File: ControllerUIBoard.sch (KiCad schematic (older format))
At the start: 32 parts

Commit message: - Earth durch GND an den letzten Stellen ersetzt
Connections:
- net labels removed: Earth
- wire segments 131 -> 135

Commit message: - BT fertig, warten auf Rueckmeldung von Microchip - CM3 fast fertig - diverse Kleinigkeiten
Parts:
- removed C? (x2): 100nF, Capacitor_SMD:C_0603_1608Metric, symbol Device:C
- removed C? (x2): 100n, Capacitor_SMD:C_0603_1608Metric, symbol Device:C
- removed C?: 4.7µF, Capacitor_SMD:CP_Elec_5x5.3, symbol Device:CP1
- removed C? (x2): 22pF, Capacitor_SMD:C_0603_1608Metric, symbol Device:C
- removed U?: CH340G, Package_SO:SOIC-16_3.9x9.9mm_P1.27mm, symbol Interface_USB:CH340G
- removed Y?: 12MHz, Crystal:Crystal_SMD_Abracon_ABM3-2Pin_5.0x3.2mm, symbol Device:Crystal
- U12, U13: renamed from U?; footprint DBV0005A_N -> (none)
- gave numbers to parts that had none: 21
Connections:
- net labels removed: ATMEGA_USB_DM, ATMEGA_USB_DP
- wire segments 135 -> 102
- no-connect marks 6 -> 0

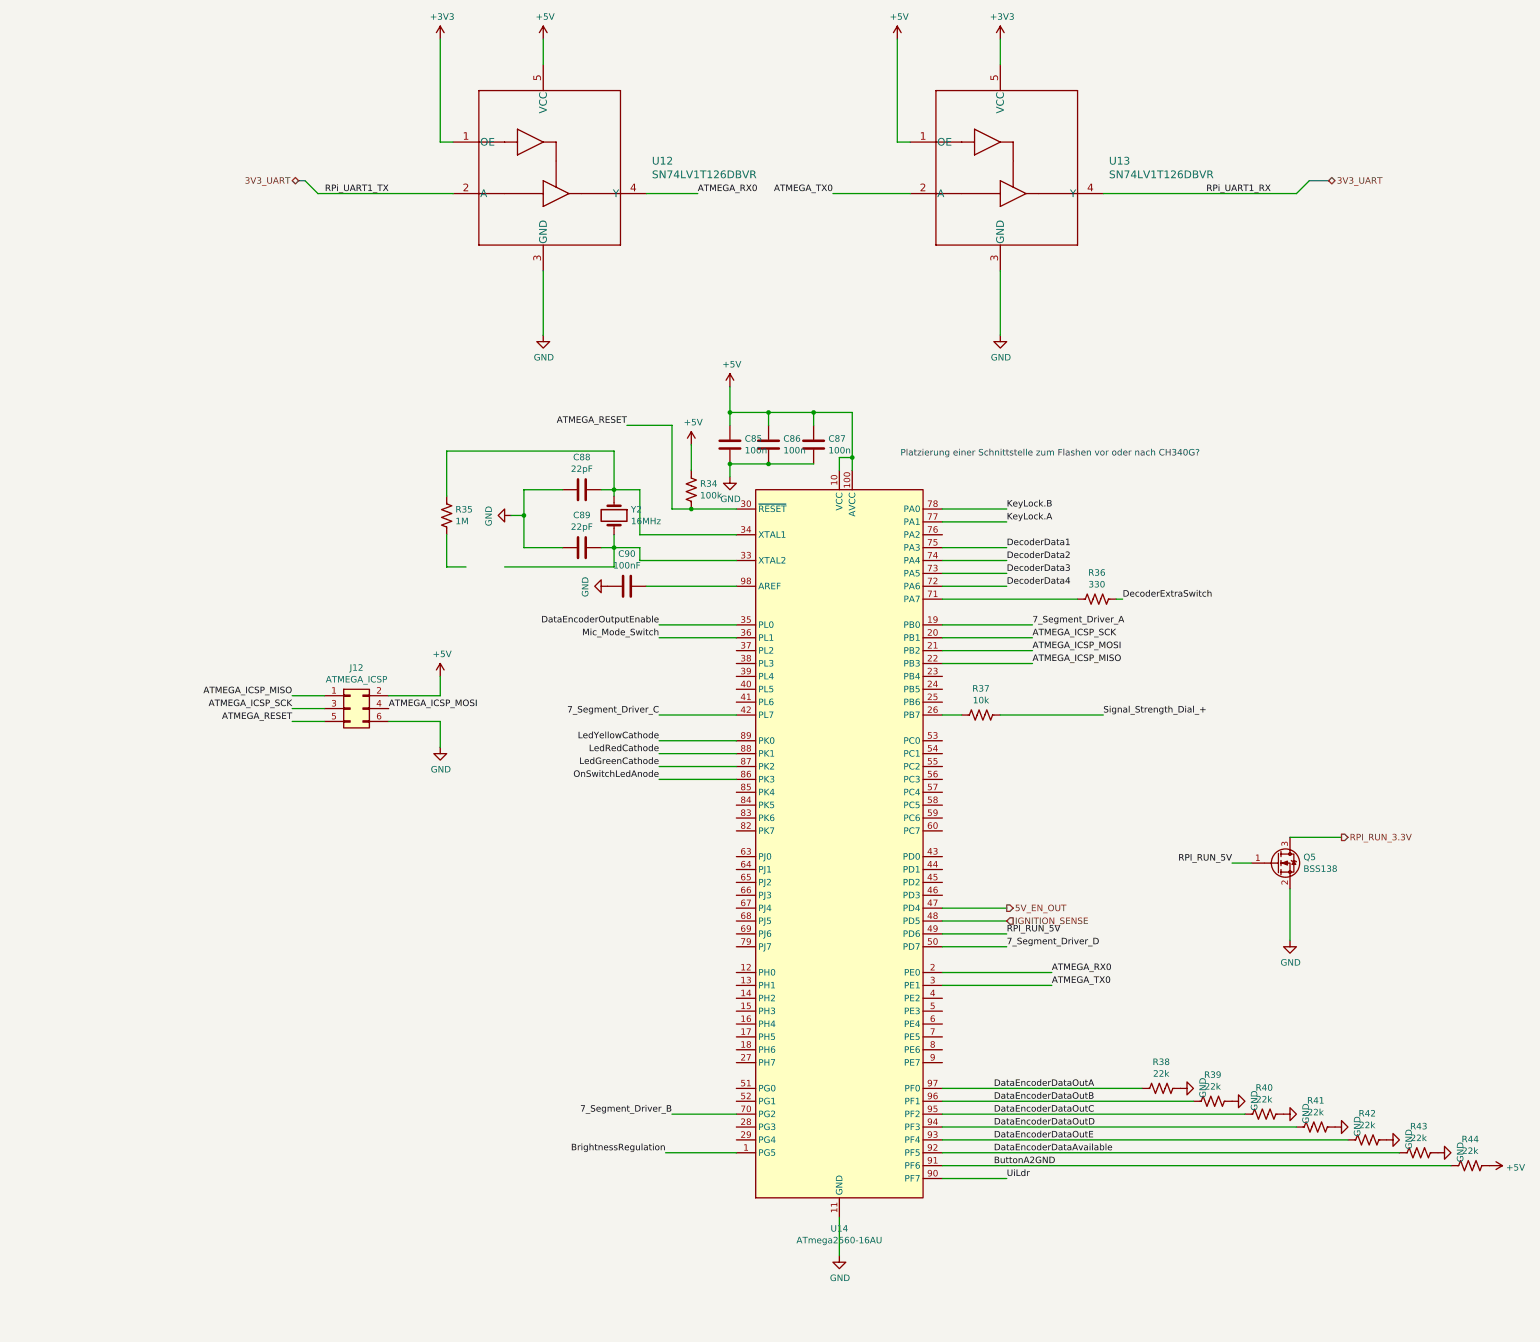
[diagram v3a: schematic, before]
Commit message: - CM3 durch CM4 ersetzt - Spannungsregler für 3,3 und 1,8V entfernt, da nun von CM4 erzeugt - RTC IC getauscht
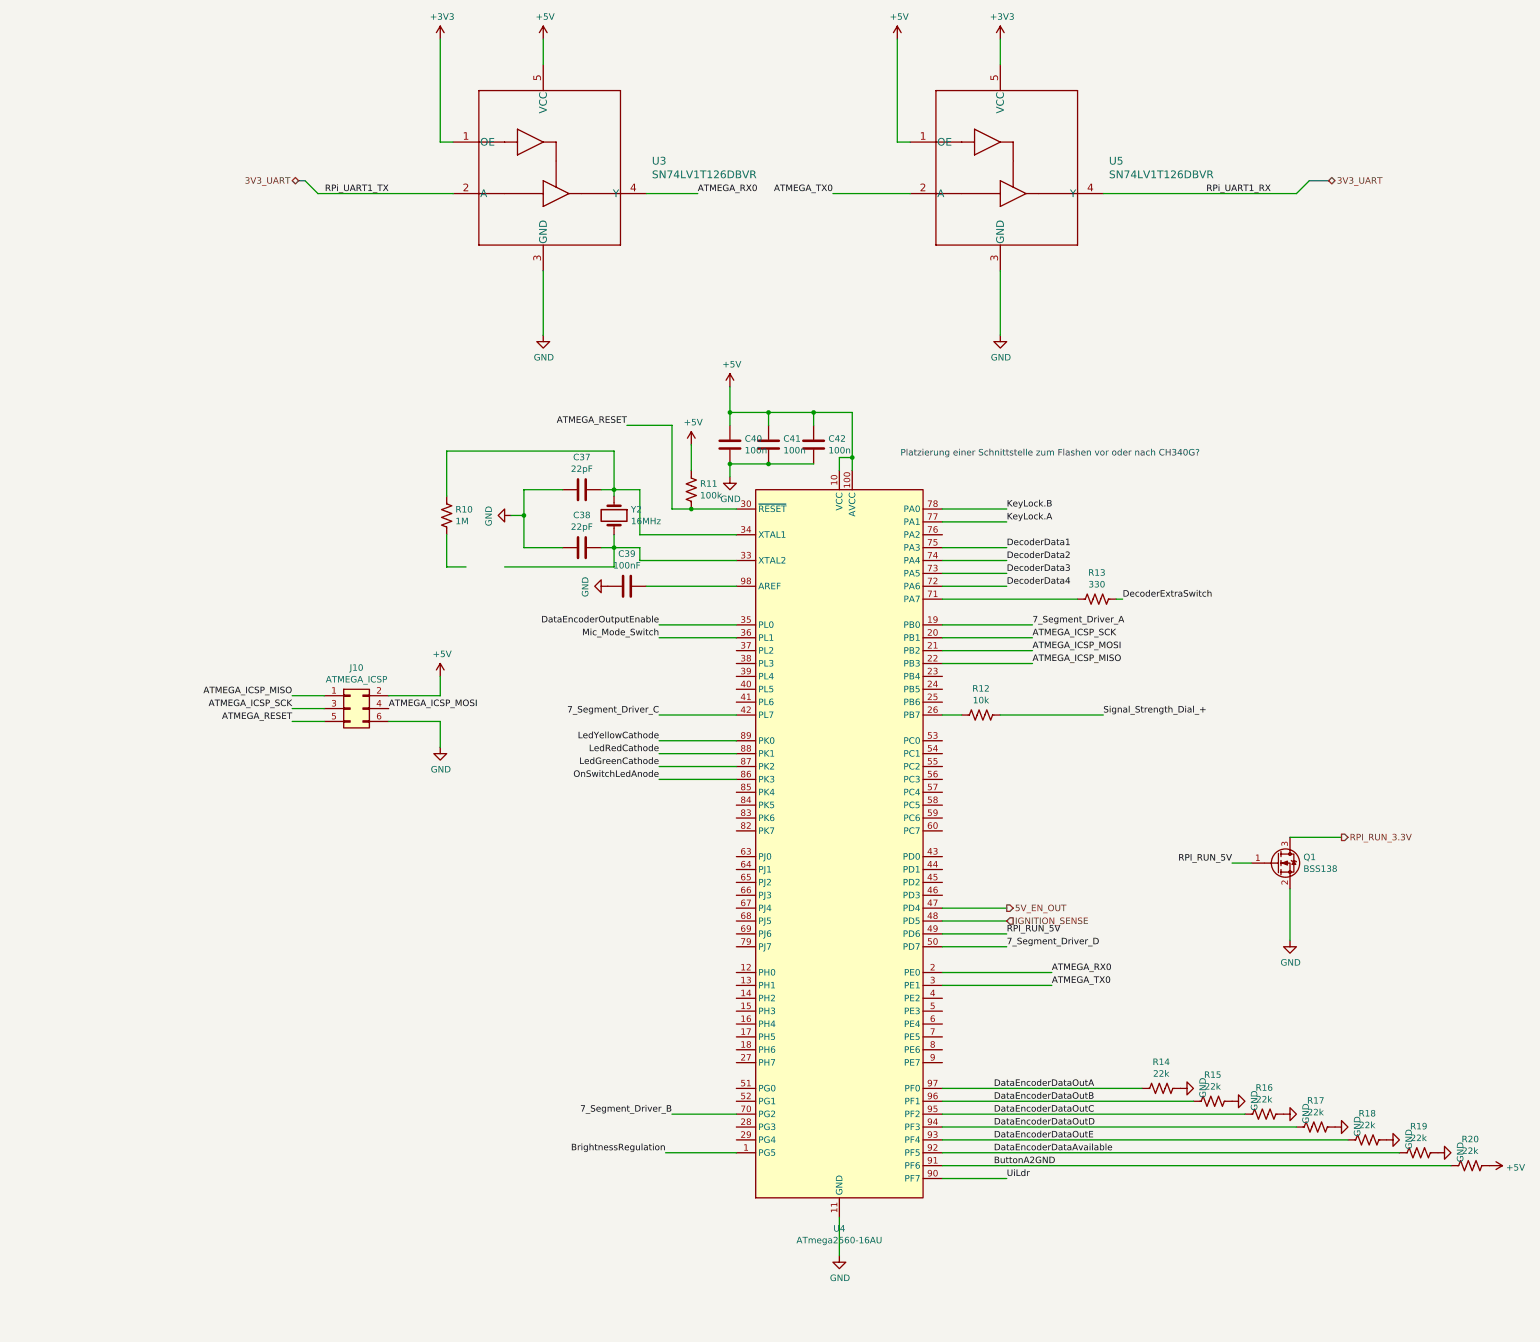
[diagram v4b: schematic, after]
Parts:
- renumbered C88 to C37, C89 to C38, C90 to C39, C85 to C40, C86 to C41, C87 to C42, J12 to J10, Q5 to Q1, R35 to R10, R34 to R11, R37 to R12, R36 to R13, R38 to R14, R39 to R15, R40 to R16, R41 to R17, R42 to R18, R43 to R19, R44 to R20, U12 to U3, U14 to U4, U13 to U5

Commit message: - Bus Topologie entfernt - Levelshifter auf eigenes Blatt, abgeschlossen
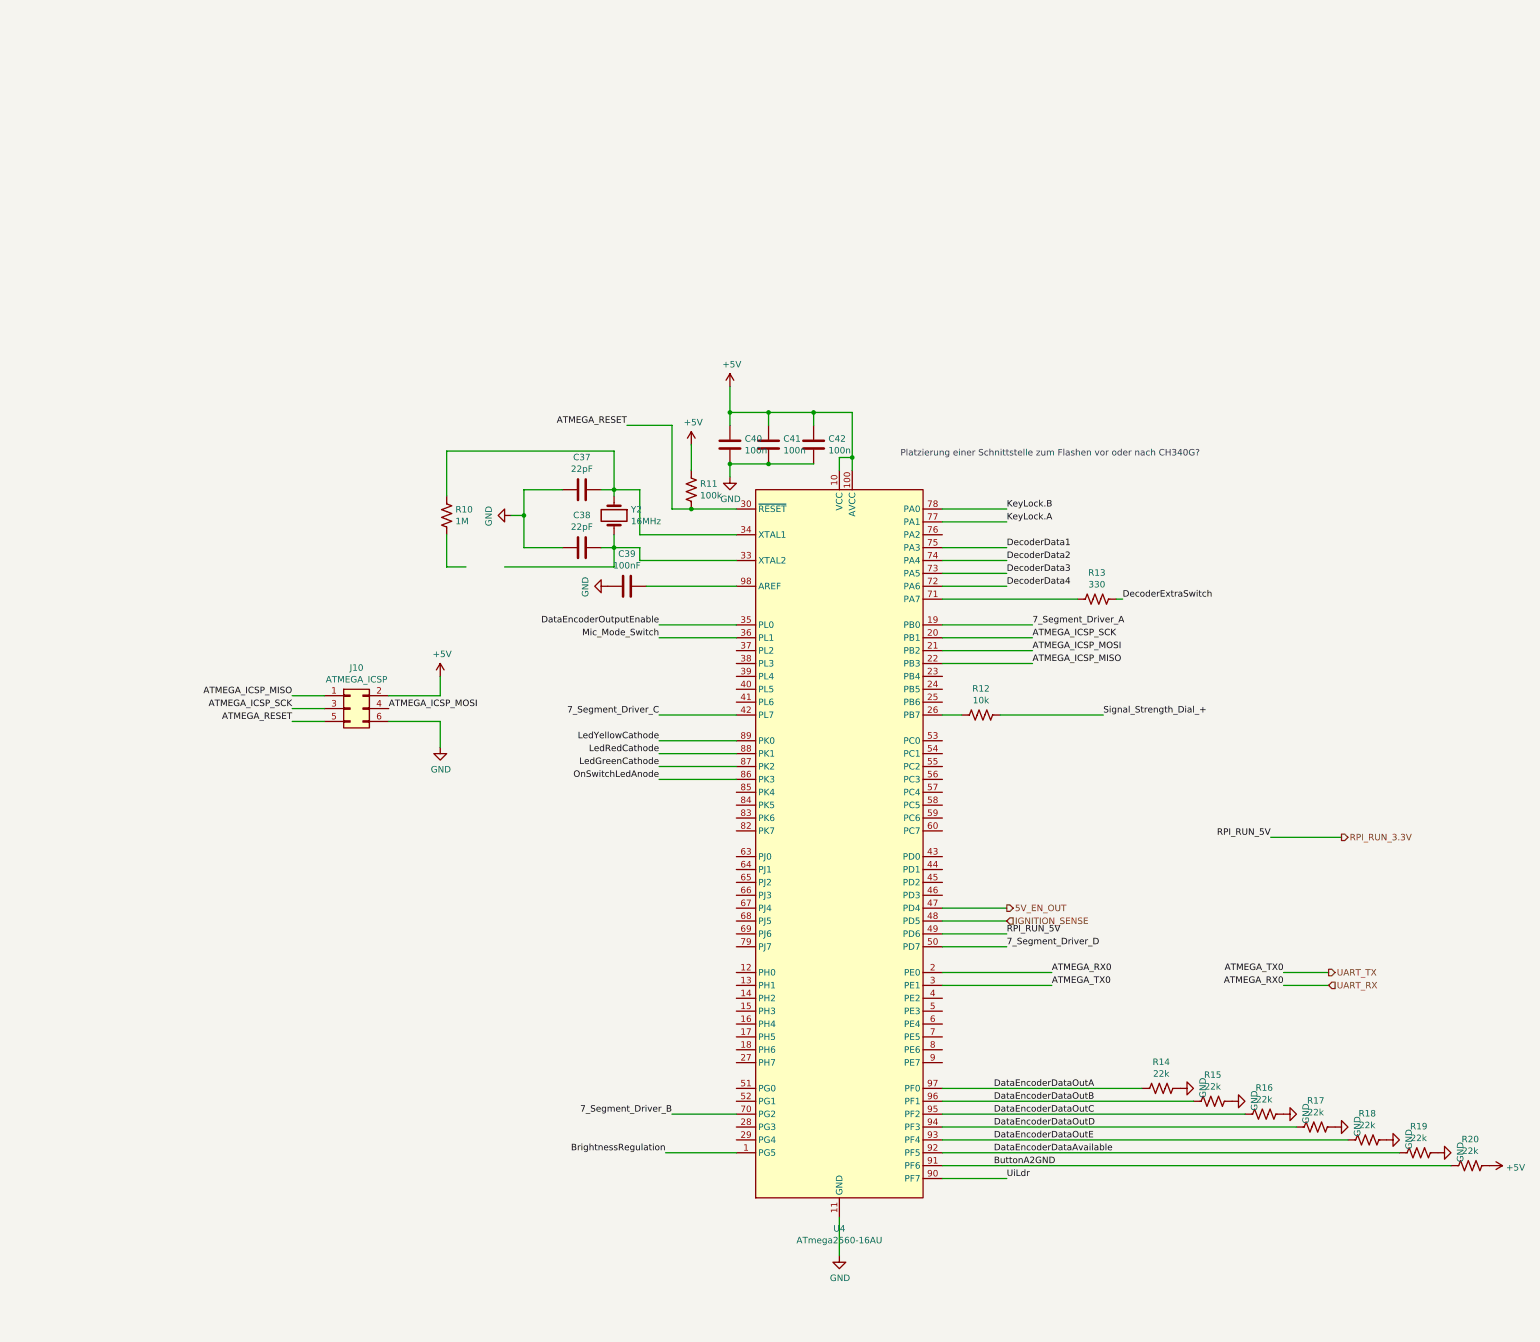
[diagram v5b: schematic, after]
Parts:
- removed Q1: BSS138, Package_TO_SOT_SMD:SOT-23, symbol Transistor_FET:BSS138
- removed U3, U5: SN74LV1T126DBVR, symbol TeKaDe:SN74LV1T126DBVR
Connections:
- net RPI_RUN_5V is gone; now on net RPI_RUN_3.3V: U4.49 (PD6)
- net ATMEGA_RX0 renamed UART_RX
- net ATMEGA_TX0 renamed UART_TX
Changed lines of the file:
@@
 $Descr A4 11693 8268
 encoding utf-8
-Sheet 4 8
+Sheet 3 9
 Title ""
 Date ""
@@
 Wire Wire Line
 	3050 2150 2900 2150
-$Comp
-L Transistor_FET:BSS138 Q1
-U 1 1 61627570
-P 9350 4450
-F 0 "Q1" H 9554 4496 50  0000 L CNN
-F 1 "BSS138" H 9554 4405 50  0000 L CNN
-F 2 "Package_TO_SOT_SMD:SOT-23" H 9550 4375 50  0001 L CIN
-F 3 "https://www.fairchildsemi.com/datasheets/BS/BSS138.pdf" H 9350 4450 50  0001 L CNN
-	1    9350 4450
-	1    0    0    -1
-$EndComp
 Text HLabel 9850 4250 2    50   Output ~ 0
 RPI_RUN_3.3V
-Wire Wire Line
-	9450 4250 9850 4250
-Text Label 9000 4450 2    50   ~ 0
+Text Label 9300 4250 2    50   ~ 0
 RPI_RUN_5V
-$Comp
-L power:GND #PWR081
-U 1 1 6163335F
-P 9450 5050
-F 0 "#PWR081" H 9450 4800 50  0001 C CNN
-F 1 "GND" H 9455 4877 50  0000 C CNN
-F 2 "" H 9450 5050 50  0001 C CNN
-F 3 "" H 9450 5050 50  0001 C CNN
-	1    9450 5050
-	1    0    0    -1
-$EndComp
-Wire Wire Line
-	9450 4650 9450 5050
-Wire Wire Line
-	9000 4450 9150 4450
 Text Label 7250 5000 0    50   ~ 0
 RPI_RUN_5V
@@
 Wire Wire Line
 	6750 4900 7250 4900
-Text Label 2450 -750 2    50   ~ 0
-RPi_UART1_TX
-Entry Wire Line
-	1800 -850 1900 -750
-Wire Bus Line
-	1800 -850 1750 -850
-Text HLabel 1750 -850 0    50   BiDi ~ 0
-3V3_UART
-$Comp
-L TeKaDe:SN74LV1T126DBVR U3
-U 1 1 60EAFEDD
-P 3650 -950
-F 0 "U3" H 4494 -897 60  0000 L CNN
-F 1 "SN74LV1T126DBVR" H 4494 -1003 60  0000 L CNN
-F 2 "" H 3650 -1010 60  0001 C CNN
-F 3 "" H 3650 -950 60  0000 C CNN
-	1    3650 -950
-	1    0    0    -1
-$EndComp
-$Comp
-L power:+5V #PWR068
-U 1 1 60EB75AD
-P 3650 -1950
-F 0 "#PWR068" H 3650 -2100 50  0001 C CNN
-F 1 "+5V" H 3665 -1777 50  0000 C CNN
-F 2 "" H 3650 -1950 50  0001 C CNN
-F 3 "" H 3650 -1950 50  0001 C CNN
-	1    3650 -1950
-	1    0    0    -1
-$EndComp
-Wire Wire Line
-	3650 -1750 3650 -1950
-$Comp
-L power:+5V #PWR075
-U 1 1 60EBD1D7
-P 6400 -1950
-F 0 "#PWR075" H 6400 -2100 50  0001 C CNN
-F 1 "+5V" H 6415 -1777 50  0000 C CNN
-F 2 "" H 6400 -1950 50  0001 C CNN
-F 3 "" H 6400 -1950 50  0001 C CNN
-	1    6400 -1950
-	1    0    0    -1
-$EndComp
-Wire Wire Line
-	2850 -1150 2950 -1150
-Wire Wire Line
-	2850 -1950 2850 -1150
-$Comp
-L power:GND #PWR069
-U 1 1 60EC6F57
-P 3650 350
-F 0 "#PWR069" H 3650 100 50  0001 C CNN
-F 1 "GND" H 3655 177 50  0000 C CNN
-F 2 "" H 3650 350 50  0001 C CNN
-F 3 "" H 3650 350 50  0001 C CNN
-	1    3650 350
-	1    0    0    -1
-$EndComp
-Wire Wire Line
-	3650 350  3650 -150
-$Comp
-L TeKaDe:SN74LV1T126DBVR U5
-U 1 1 60EDF3D9
-P 7200 -950
-F 0 "U5" H 8044 -897 60  0000 L CNN
-F 1 "SN74LV1T126DBVR" H 8044 -1003 60  0000 L CNN
-F 2 "" H 7200 -1010 60  0001 C CNN
-F 3 "" H 7200 -950 60  0000 C CNN
-	1    7200 -950
-	1    0    0    -1
-$EndComp
-Wire Wire Line
-	7200 -1750 7200 -1950
-Wire Wire Line
-	6400 -1150 6500 -1150
-Wire Wire Line
-	6400 -1950 6400 -1150
-$Comp
-L power:GND #PWR077
-U 1 1 60EDF3EE
-P 7200 350
-F 0 "#PWR077" H 7200 100 50  0001 C CNN
-F 1 "GND" H 7205 177 50  0000 C CNN
-F 2 "" H 7200 350 50  0001 C CNN
-F 3 "" H 7200 350 50  0001 C CNN
-	1    7200 350
-	1    0    0    -1
-$EndComp
-Wire Wire Line
-	7200 350  7200 -150
-$Comp
-L power:+3V3 #PWR076
-U 1 1 60EF02E8
-P 7200 -1950
-F 0 "#PWR076" H 7200 -2100 50  0001 C CNN
-F 1 "+3V3" H 7215 -1777 50  0000 C CNN
-F 2 "" H 7200 -1950 50  0001 C CNN
-F 3 "" H 7200 -1950 50  0001 C CNN
-	1    7200 -1950
-	1    0    0    -1
-$EndComp
-$Comp
-L power:+3V3 #PWR064
-U 1 1 60EF0C4F
-P 2850 -1950
-F 0 "#PWR064" H 2850 -2100 50  0001 C CNN
-F 1 "+3V3" H 2865 -1777 50  0000 C CNN
-F 2 "" H 2850 -1950 50  0001 C CNN
-F 3 "" H 2850 -1950 50  0001 C CNN
-	1    2850 -1950
-	1    0    0    -1
-$EndComp
-Text Label 8800 -750 0    50   ~ 0
-RPi_UART1_RX
-Entry Wire Line
-	9600 -850 9500 -750
-Text HLabel 9750 -850 2    50   BiDi ~ 0
-3V3_UART
-Wire Bus Line
-	9600 -850 9750 -850
-Wire Wire Line
-	8000 -750 9500 -750
-Text Label 4850 -750 0    50   ~ 0
+Text Label 9400 5400 2    50   ~ 0
 ATMEGA_RX0
-Text Label 5900 -750 2    50   ~ 0
+Text Label 9400 5300 2    50   ~ 0
 ATMEGA_TX0
 Wire Wire Line
-	4850 -750 4450 -750
-Wire Wire Line
-	5900 -750 6500 -750
-Wire Wire Line
-	1900 -750 2950 -750
+	9400 5400 9750 5400
 $Comp
 L power:GND #PWR074
@@
 	0    -1   -1   0
 $EndComp
+Wire Wire Line
+	9300 4250 9850 4250
+Wire Wire Line
+	9750 5300 9400 5300
+Text HLabel 9750 5400 2    50   Input ~ 0
+UART_RX
+Text HLabel 9750 5300 2    50   Output ~ 0
+UART_TX
 $EndSCHEMATC
